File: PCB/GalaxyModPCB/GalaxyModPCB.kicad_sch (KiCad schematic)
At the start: 64 parts, among them J1 LED RGBW Connector, J2 USB to UART, J3 Motor Connector, J4 Projector Connector, J5 Debugging Header, J6 Power Header, Q1 IRLML0030, Q2 IRLML0030, Q3 IRLML0030, Q4 IRLML0030, Q5 IRLML0030, Q6 IRLML0030, SW1 On/Off, SW2 Colour, SW3 Brightness, SW4 Motor, U1 ESP32-WROOM-32, U2 AMS1117-3.3

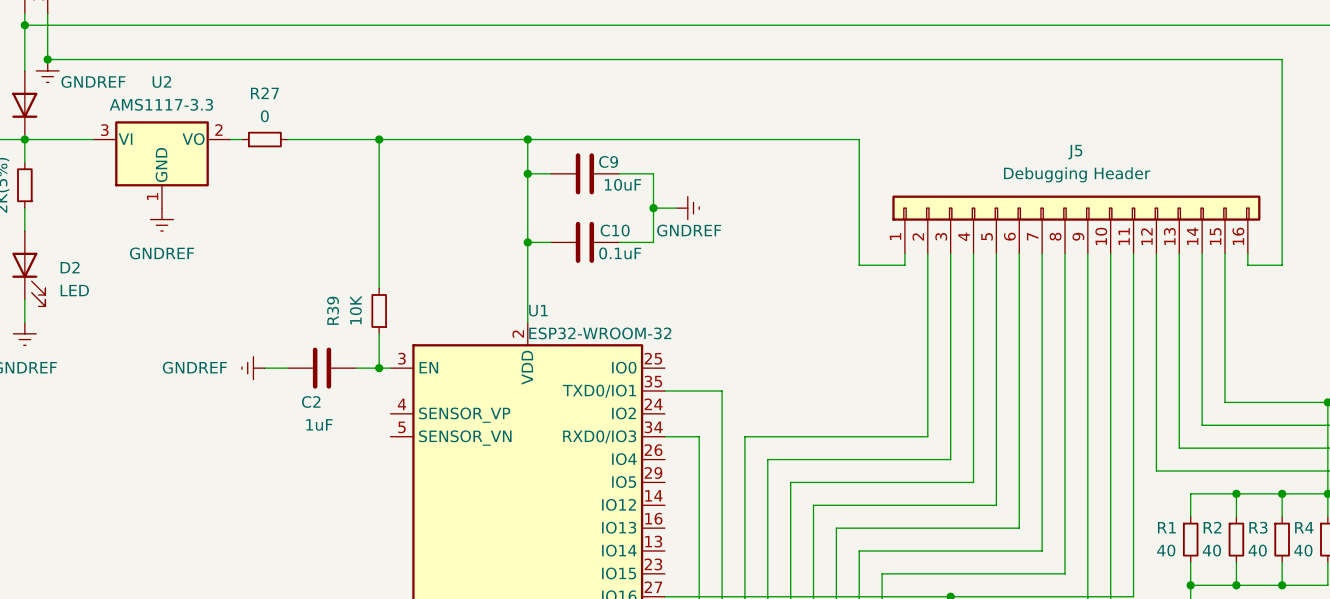
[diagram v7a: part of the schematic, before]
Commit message: Assigned footprints
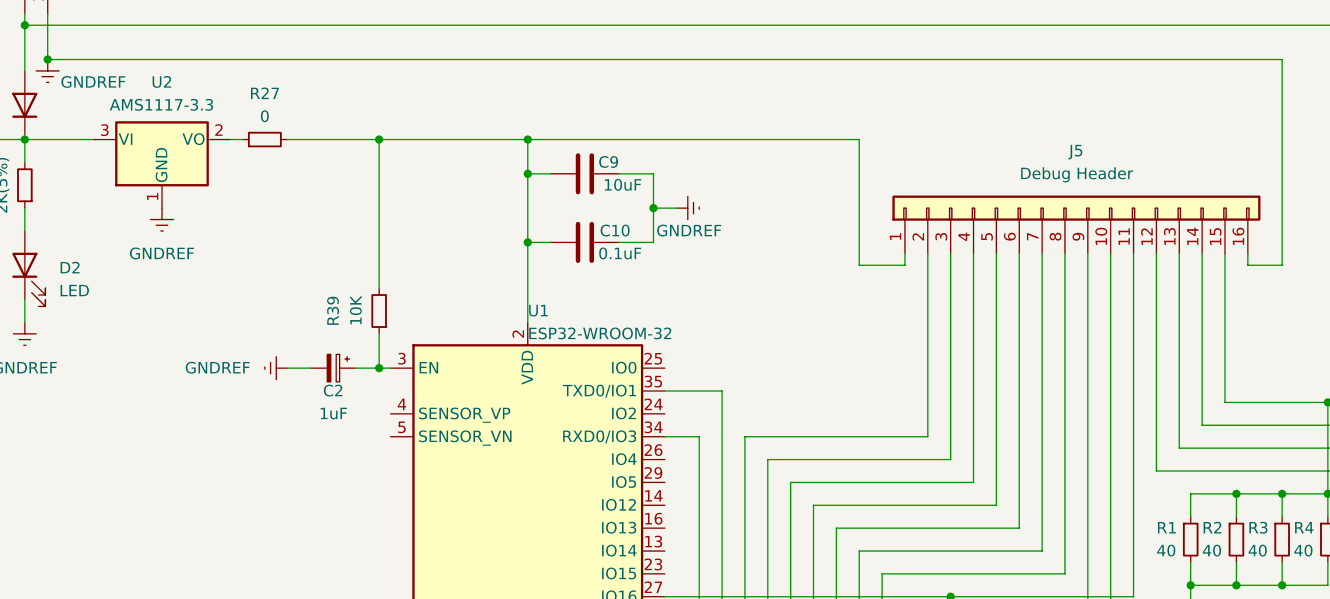
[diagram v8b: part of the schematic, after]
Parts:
- removed C2: 1uF, symbol Device:C
- added C2: 1uF, Capacitor_THT:CP_Radial_D4.0mm_P1.50mm, symbol Device:C_Polarized_Small
- C10, C4, C5, C6, C7, C8, C9: footprint (none) -> Capacitor_SMD:C_0805_2012Metric
- J5: value Debugging Header -> Debug Header
- SW1, SW2, SW3, SW4: footprint (none) -> Button_Switch_SMD:SW_Push_1P1T_NO_6x6mm_H9.5mm
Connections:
- net GNDREF: now also C2.2
- net at R39.1, U1.3 (EN): now also C2.1
